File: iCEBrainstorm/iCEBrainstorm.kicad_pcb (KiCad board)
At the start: 4 copper layers, 80 x 70 mm, 117 parts, among them J1 Connector, USB-TYPE-C-16P, J10 Conn_01x02_Pin, J11 Conn_01x06_Pin, J12 Connector, USB-TYPE-C-16P, J2 Conn_01x06_Pin, J3 Conn_01x16_Pin, J6 Conn_01x03_Pin, J7 Conn_01x03_Pin, J8 Conn_01x02_Pin, J9 Conn_01x02_Pin, Q1 HL2312, SW1 SW_DIP_x08, U1 AMS1117-3.3, U2 AMS1117-1.2, U3 STM32F412RETx, U4 ICE40UP5K-SG48ITR, U5 W25Q128, X1 16 MHz

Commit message: gekocht mit luci
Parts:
- added C33: 100nF, PCM_JLCPCB:C_0603, F.Cu at (84.0, 113.9)
- added C34: 100nF, PCM_JLCPCB:C_0603, F.Cu at (80.8, 114.6)
- added R21: 1.5kΩ, PCM_JLCPCB:R_0603, F.Cu at (84.0, 110.4)
- added R22: 1.5kΩ, PCM_JLCPCB:R_0603, F.Cu at (77.5, 113.9)
- added R23: 1.5kΩ, PCM_JLCPCB:R_0603, F.Cu at (77.5, 110.4)
- added R24: 1.5kΩ, PCM_JLCPCB:R_0603, F.Cu at (80.8, 107.9)
- added U6: LSM6DS3, Package_LGA:LGA-14_3x2.5mm_P0.5mm_LayoutBorder3x4y, F.Cu at (80.8, 111.6)
- moved J11 113.5 mm to (69.8, 118.1), turned to 180 degrees
- moved D3 111.5 mm to (96.5, 68.6), turned to 90 degrees
- moved D2 108.7 mm to (99.1, 68.6), turned to 90 degrees
- moved D1 106.1 mm to (101.6, 68.6), turned to 90 degrees
- moved R6 104.0 mm to (96.5, 72.4), turned to -90 degrees
- moved D4 103.7 mm to (104.1, 68.6), turned to 90 degrees
- moved R5 101.6 mm to (99.1, 72.4), turned to -90 degrees
- moved R2 99.4 mm to (101.6, 72.4), turned to -90 degrees
- moved R30 97.4 mm to (104.1, 72.4), turned to 90 degrees
- moved J3 95.1 mm to (66.0, 80.0), turned to 0 degrees
- moved Q1 93.6 mm to (100.3, 76.2), turned to 90 degrees
- moved R1 88.2 mm to (100.3, 80.0), turned to 0 degrees
- moved C11 84.4 mm to (49.1, 22.2)
- moved C13 84.4 mm to (38.0, 20.0)
- moved C14 84.4 mm to (46.1, 38.2)
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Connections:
- U3 pad 50: /FPGA_BUS0 -> unconnected-(U3-PA15-Pad50)
- U3 pad 54: /FPGA_BUS1 -> unconnected-(U3-PD2-Pad54)
- U4 pad 10: unconnected-(U4B-IOB_18a-Pad10) -> /SPI2_SCK
- U4 pad 11: unconnected-(U4B-IOB_20a-Pad11) -> /SPI2_NSS
- U4 pad 23: /FPGA_BUS0 -> unconnected-(U4A-IOT_37a-Pad23)
- U4 pad 25: /FPGA_BUS1 -> unconnected-(U4A-IOT_36b-Pad25)
- U4 pad 28: /SPI2_MOSI -> unconnected-(U4A-IOT_41a-Pad28)
- U4 pad 31: /SPI2_MISO -> unconnected-(U4A-IOT_42b-Pad31)
- U4 pad 32: /SPI2_SCK -> unconnected-(U4A-IOT_43a-Pad32)
- U4 pad 34: /SPI2_NSS -> unconnected-(U4A-IOT_44b-Pad34)
- U4 pad 4: unconnected-(U4C-IOB_8a-Pad4) -> /SPI2_MOSI
- U4 pad 6: unconnected-(U4B-IOB_13b-Pad6) -> /SPI2_MISO
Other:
- board text added: "RESET STM"

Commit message: wider mit luci gekocht
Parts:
- moved C11 86.7 mm to (92.7, 97.2), turned to -135 degrees
- moved C16 86.4 mm to (81.8, 104.4)
- moved C18 86.4 mm to (81.8, 99.5)
- moved FB1 86.4 mm to (81.8, 102.0)
- moved C19 83.4 mm to (84.8, 97.5), turned to -135 degrees
- moved C8 81.3 mm to (98.3, 91.9), turned to -135 degrees
- moved C13 81.0 mm to (92.6, 79.9), turned to -45 degrees
- moved C14 75.7 mm to (97.3, 94.0), turned to 135 degrees
- moved R16 74.6 mm to (81.3, 78.7), turned to -90 degrees
- moved R15 73.0 mm to (79.8, 78.7), turned to -90 degrees
- moved R39 68.8 mm to (89.5, 74.3)
- moved D13 68.4 mm to (89.5, 78.1)
- moved C15 65.7 mm to (78.9, 90.3)
- moved C29 48.8 mm to (108.6, 80.0), turned to 90 degrees
- moved R7 48.0 mm to (123.4, 91.2)
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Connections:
- J3 pad 1: /PC0 -> /PA15
- J3 pad 10: +3V3 -> /PC15
- J3 pad 11: /PC10 -> /PC0
- J3 pad 12: /PC11 -> /PC1
- J3 pad 13: /PC12 -> /PC2
- J3 pad 14: /PC13 -> /PC3
- J3 pad 15: /PC14 -> /PA0
- J3 pad 16: /PC15 -> /PA1
- J3 pad 2: /PC1 -> /PC10
- J3 pad 3: /PC2 -> /PC11
- J3 pad 4: /PC3 -> /PC12
- J3 pad 5: /PC4 -> /PD2
- J3 pad 6: /PC5 -> /PB4
- J3 pad 7: /PC6 -> /PB9
- J3 pad 8: /PC7 -> /PC13
- J3 pad 9: /PC8 -> /PC14
- J8 pad 1: /FPGA_GLOBAL_3 -> unconnected-(J8-Pin_1-Pad1)
- J8 pad 2: /FPGA_GLOBAL_6 -> unconnected-(J8-Pin_2-Pad2)
- R18 pad 2: /IN1 -> /FPGA_GLOBAL_0
- R20 pad 2: /IN3 -> /FPGA_GLOBAL_1
- R25 pad 1: Net-(U4B-IOB_22a) -> /FPGA_GLOBAL_6
- R26 pad 1: Net-(U4B-IOB_22a) -> /FPGA_GLOBAL_6
- SW1 pad 6: /IN1 -> /FPGA_GLOBAL_0
- SW1 pad 8: /IN3 -> /FPGA_GLOBAL_1
- U3 pad 14: unconnected-(U3-PA0-Pad14) -> /PA0
- U3 pad 15: unconnected-(U3-PA1-Pad15) -> /PA1
- U3 pad 24: /PC4 -> unconnected-(U3-PC4-Pad24)
- U3 pad 25: /PC5 -> unconnected-(U3-PC5-Pad25)
- U3 pad 29: /FPGA_CLK -> /FPGA_GLOBAL_0
- U3 pad 37: /PC6 -> unconnected-(U3-PC6-Pad37)
- U3 pad 38: /PC7 -> unconnected-(U3-PC7-Pad38)
- U3 pad 39: /PC8 -> unconnected-(U3-PC8-Pad39)
- U3 pad 50: unconnected-(U3-PA15-Pad50) -> /PA15
- U3 pad 54: unconnected-(U3-PD2-Pad54) -> /PD2
- U3 pad 56: unconnected-(U3-PB4-Pad56) -> /PB4
- U3 pad 62: unconnected-(U3-PB9-Pad62) -> /PB9
- U4 pad 12: Net-(U4B-IOB_22a) -> unconnected-(U4B-IOB_22a-Pad12)
- U4 pad 13: /FUD- -> unconnected-(U4B-IOB_24a-Pad13)
- U4 pad 2: /OUT1 -> /USART1_RX
- U4 pad 20: /FPGA_GLOBAL_3 -> /FPGA_CLK
- U4 pad 21: /FUD+ -> unconnected-(U4B-IOB_23b-Pad21)
- U4 pad 25: unconnected-(U4A-IOT_36b-Pad25) -> /OUT0
- U4 pad 26: /USART1_RX -> /OUT1
- U4 pad 27: /USART1_TX -> /OUT2
- U4 pad 28: unconnected-(U4A-IOT_41a-Pad28) -> /OUT3
- U4 pad 3: /OUT0 -> /USART1_TX
- U4 pad 31: unconnected-(U4A-IOT_42b-Pad31) -> /BTN0
- U4 pad 32: unconnected-(U4A-IOT_43a-Pad32) -> /BTN1
- U4 pad 34: unconnected-(U4A-IOT_44b-Pad34) -> /IN0
- U4 pad 35: /FPGA_CLK -> /FPGA_GLOBAL_0
- U4 pad 36: /BTN0 -> /IN2
- U4 pad 38: /BTN1 -> unconnected-(U4A-IOT_50b-Pad38)
- U4 pad 45: unconnected-(U4C-IOB_5b-Pad45) -> /FUD-
- U4 pad 47: /OUT3 -> unconnected-(U4C-IOB_2a-Pad47)
- U4 pad 48: /OUT2 -> /FUD+
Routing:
- net GND: track 0.00 -> 82.8 mm, vias 0 -> 15
- net +3V3: track 0.00 -> 54.4 mm, vias 0 -> 9
- net /PA1: track 0.00 -> 33.6 mm, vias 0 -> 1
- net /PC3: track 0.00 -> 32.3 mm, vias 0 -> 1
- net /PA0: track 0.00 -> 31.3 mm, vias 0 -> 1
- net /PD2: track 0.00 -> 28.6 mm, vias 0 -> 1
- net /PB4: track 0.00 -> 28.6 mm, vias 0 -> 1
- net /PC11: track 0.00 -> 28.4 mm, vias 0 -> 1
- net /PC10: track 0.00 -> 28.4 mm, vias 0 -> 1
- net /PC12: track 0.00 -> 28.2 mm, vias 0 -> 1
- net /PC2: track 0.00 -> 28.2 mm, vias 0 -> 1
- net VBUS: track 0.00 -> 27.9 mm, vias 0 -> 8
- net /PA15: track 0.00 -> 27.6 mm, vias 0 -> 1
- net /PC1: track 0.00 -> 25.8 mm, vias 0 -> 1
- net /PC0: track 0.00 -> 24.6 mm, vias 0 -> 1
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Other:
- board text added: "OUT_STM"
- board text added: "PA0"
- board text added: "PA1"
- board text added: "PA15"
- board text added: "PB4"
- board text added: "PB9"
- board text added: "PD2"
- board text removed: "FPGA"
- board text removed: "G3"
- board text removed: "G6"
- board text removed: "OUT8"
- board text removed: "PC4"
- board text removed: "PC5"
- board text removed: "PC6"
- board text removed: "PC7"
- board text removed: "PC8"

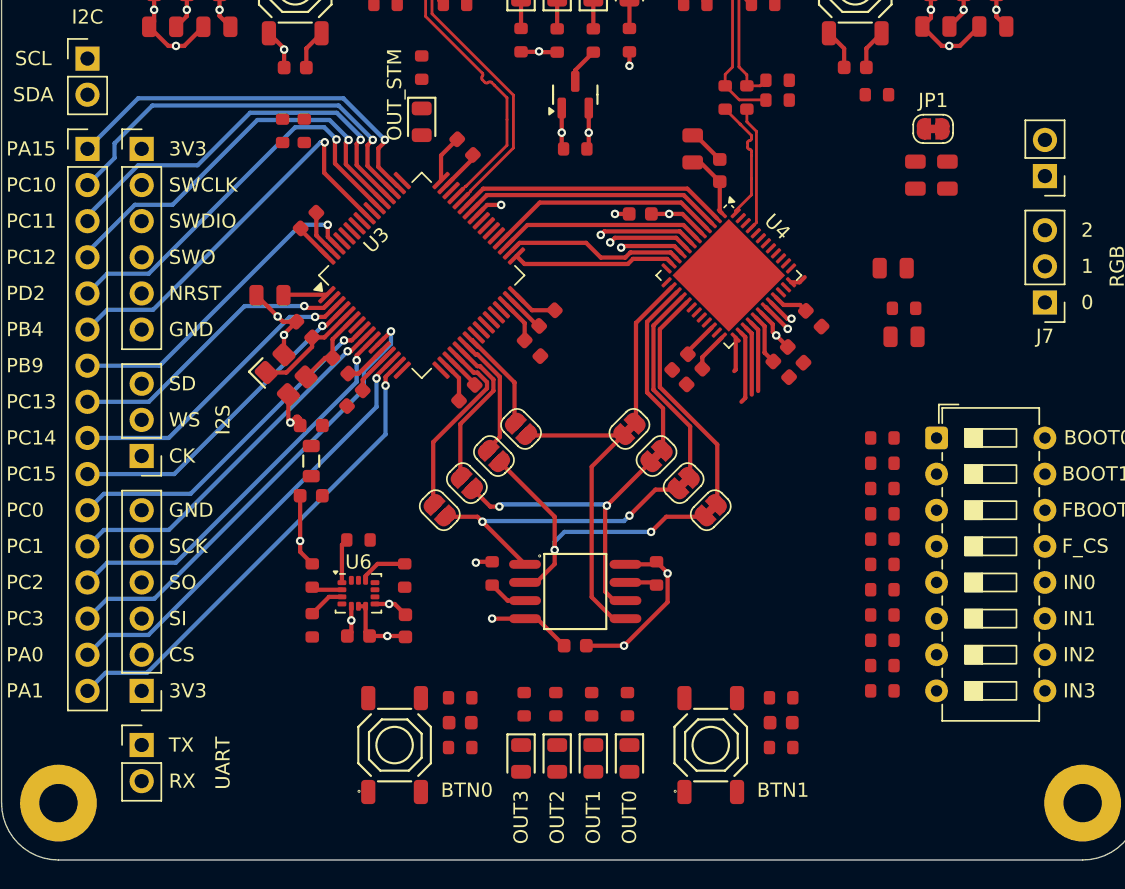
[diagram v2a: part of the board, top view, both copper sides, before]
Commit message: did some lines + added a IN connector :)
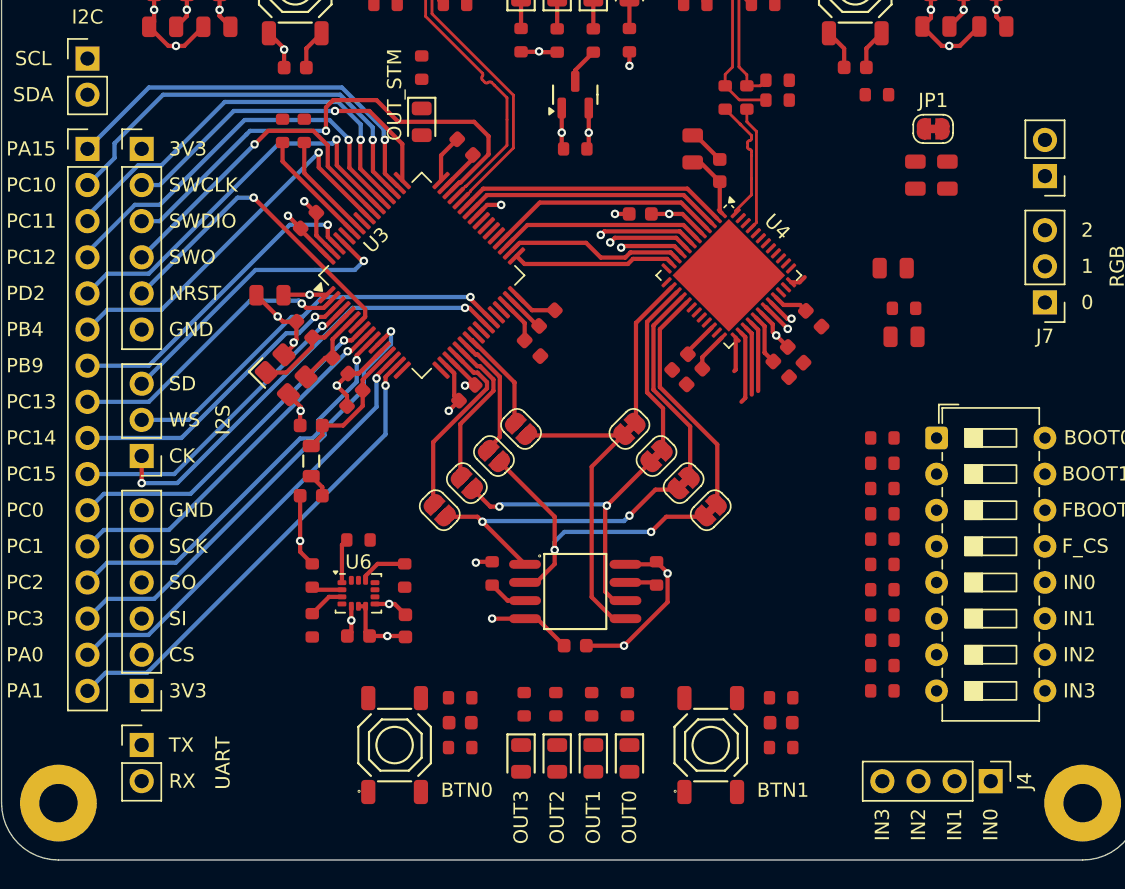
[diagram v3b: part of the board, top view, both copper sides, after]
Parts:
- added J4: Conn_01x04_Pin, Connector_PinHeader_2.54mm:PinHeader_1x04_P2.54mm_Vertical, F.Cu at (129.5, 124.5)
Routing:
- net /SWDIO: track 0.00 -> 34.9 mm, vias 0 -> 1
- net /I2S5_CK: track 0.00 -> 31.7 mm, vias 0 -> 2
- net /I2S5_WS: track 0.00 -> 28.9 mm, vias 0 -> 1
- net /SWCLK: track 0.00 -> 24.0 mm, vias 0 -> 1
- net /NRST: track 2.86 -> 25.9 mm, vias 0 -> 1
- net /SWO: track 0.00 -> 23.1 mm, vias 0 -> 1
- net /I2S5_SD: track 0.00 -> 21.3 mm, vias 0 -> 1
- net /I2C1_SDA: track 0.00 -> 8.23 mm
- net /I2C1_SCL: track 0.00 -> 7.39 mm
- net +3.3VA: track 3.20 -> 9.46 mm
- net GND: track 82.8 -> 87.1 mm, vias 15 -> 18
- net +3V3: track 54.4 -> 58.1 mm, vias 9 -> 12
- net /PB4: track 28.6 -> 27.3 mm
- net /PC11: track 28.4 -> 29.4 mm
- net /PC10: track 28.4 -> 29.3 mm
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
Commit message: did back silkscreen design
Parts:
- added REF**: iCE-Brain, JJ:iCE-Brain, F.Cu at (100.8, 96.1)

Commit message: added uart1 connector, added power connectors, added schema back silkscreen symbol
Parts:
- removed REF**: iCE-Brain, JJ:iCE-Brain
- added J13: Conn_01x02_Pin, Connector_PinHeader_2.54mm:PinHeader_1x02_P2.54mm_Vertical, F.Cu at (157.5, 131.4)
- added J14: Conn_01x02_Pin, Connector_PinHeader_2.54mm:PinHeader_1x02_P2.54mm_Vertical, F.Cu at (157.5, 139.1)
- added J15: Conn_01x02_Pin, Connector_PinHeader_2.54mm:PinHeader_1x02_P2.54mm_Vertical, F.Cu at (157.5, 146.7)
- added J5: Conn_01x02_Pin, Connector_PinHeader_2.54mm:PinHeader_1x02_P2.54mm_Vertical, F.Cu at (104.1, 80.6)
- added N1: Housing, iCE-Brain Silkscreen, JJ:iCE-Brain, F.Cu at (101.0, 96.1)
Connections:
- U3 pad 24: unconnected-(U3-PC4-Pad24) -> /FPGA_BUS1
- U3 pad 25: unconnected-(U3-PC5-Pad25) -> /FPGA_BUS0
- U4 pad 12: unconnected-(U4B-IOB_22a-Pad12) -> /FPGA_BUS0
- U4 pad 13: unconnected-(U4B-IOB_24a-Pad13) -> /FPGA_BUS1
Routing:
- net /FPGA_BUS1: track 0.00 -> 17.5 mm
- net /FPGA_BUS0: track 0.00 -> 17.3 mm
- net /USART1_RX: track 19.0 -> 25.8 mm
- net /USART1_TX: track 18.2 -> 22.6 mm, vias 0 -> 1
- net +3V3: vias 12 -> 13
- net GND: vias 18 -> 19
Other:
- board text added: "UART1"
- board text added: "UART2"
- board text removed: "UART"

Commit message: did some routing
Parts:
- removed J8: Conn_01x02_Pin, Connector_PinHeader_2.54mm:PinHeader_1x02_P2.54mm_Vertical
- moved J13 88.0 mm to (69.8, 123.2)
- moved J14 63.8 mm to (133.3, 80.0)
- moved J15 59.1 mm to (133.3, 92.7)
- moved C9 10.3 mm to (114.8, 98.8), turned to -90 degrees
- moved R7 9.46 mm to (116.7, 97.9), turned to 90 degrees
- moved C22 6.16 mm to (128.8, 76.1), turned to 0 degrees
- moved C5 5.74 mm to (128.8, 78.4), turned to 0 degrees
- moved C23 4.19 mm to (121.7, 92.5), turned to -90 degrees
- moved J10 3.81 mm to (69.8, 118.1)
- moved J11 2.54 mm to (69.8, 115.6)
- moved JP1 1.46 mm to (125.6, 77.1), turned to -90 degrees
- moved J9 1.27 mm to (66.0, 74.9)
- moved J6 1.27 mm to (69.8, 100.3)
- moved J7 0.64 mm to (133.3, 90.2)
- moved C26 0.28 mm to (115.6, 94.4)
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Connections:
- U3 pad 41: /FPGA_GLOBAL_1 -> /FPGA_GLOBAL_6
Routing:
- net /I2C1_SCL: track 7.39 -> 82.7 mm, vias 0 -> 6
- net /I2C1_SDA: track 8.23 -> 79.0 mm, vias 0 -> 4
- net /BTN0: track 2.16 -> 65.3 mm, vias 1 -> 0
- net /BOOT0: track 0.00 -> 52.9 mm, vias 0 -> 1
- net /IN0: track 0.00 -> 50.4 mm, vias 0 -> 1
- net /FPGA_GLOBAL_0: track 0.00 -> 49.5 mm, vias 0 -> 1
- net /IN2: track 1.11 -> 50.2 mm, vias 0 -> 1
- net /FPGA_GLOBAL_1: track 2.07 -> 49.1 mm
- net /FPGA_SPI_CS: track 21.5 -> 68.4 mm
- net /BOOT1: track 0.00 -> 42.1 mm, vias 0 -> 1
- net /OUT3: track 5.03 -> 46.3 mm
- net /OUT2: track 4.89 -> 42.4 mm
- net /USART2_RX: track 0.00 -> 33.8 mm, vias 0 -> 1
- net /BTN1: track 1.92 -> 35.6 mm, vias 1 -> 0
- net /OUT1: track 5.11 -> 38.5 mm
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- added copper zone on In2.Cu, net +3V3
- added copper zone on In1.Cu, net GND

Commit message: fertig
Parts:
- added J11: Conn_01x04_Pin, Connector_PinHeader_2.54mm:PinHeader_1x04_P2.54mm_Vertical, F.Cu at (133.3, 74.9)
- moved J5 10.2 mm to (133.3, 69.8)
- renumbered D13 to D9, J7 to J10, J9 to J12, J10 to J13, J5 to J14, J11 to J15, J12 to J16, J3 to J2, J2 to J3, J13 to J4, J14 to J5, J15 to J6, J4 to J7, J6 to J9, JP8 to JP6, JP9 to JP7, JP10 to JP8, JP11 to JP9, R17 to R11, R18 to R12, R19 to R13, R20 to R14, R11 to R15, R12 to R16, R13 to R17, R14 to R18, R15 to R19, R16 to R20, R29 to R21, R30 to R22, R31 to R23, R32 to R24, R33 to R25, R34 to R26, R39 to R27, R40 to R28, R41 to R29, R42 to R30, R43 to R31, R44 to R32, R45 to R33, R24 to R34, R23 to R35, R22 to R36, R46 to R37, R47 to R38, R25 to R39, R26 to R40, R21 to R41, R27 to R42, R28 to R43
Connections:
- R39 pad 1: /FPGA_GLOBAL_6 -> /FUPP
- R40 pad 1: /FPGA_GLOBAL_6 -> /FUPP
- U3 pad 29: /FPGA_GLOBAL_0 -> unconnected-(U3-PB10-Pad29)
- U4 pad 23: unconnected-(U4A-IOT_37a-Pad23) -> /FPGA_IO_3
- U4 pad 38: unconnected-(U4A-IOT_50b-Pad38) -> /FPGA_IO_2
- U4 pad 42: unconnected-(U4A-IOT_51a-Pad42) -> /FPGA_IO_1
- U4 pad 43: unconnected-(U4A-IOT_49a-Pad43) -> /FUPP
- U4 pad 47: unconnected-(U4C-IOB_2a-Pad47) -> /FPGA_IO_0
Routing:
- net +1V2: track 24.2 -> 100.0 mm
- net VBUS: track 27.9 -> 97.9 mm
- net /FPGA_BOOT: track 8.34 -> 49.1 mm
- net /FPGA_IO_3: track 0.00 -> 30.0 mm, vias 0 -> 3
- net /FPGA_IO_0: track 0.00 -> 26.8 mm, vias 0 -> 1
- net +2V5: track 6.66 -> 30.6 mm
- net /FPGA_IO_1: track 0.00 -> 23.4 mm
- net /FPGA_IO_2: track 0.00 -> 21.6 mm, vias 0 -> 1
- net /FUPP: track 0.00 -> 11.9 mm
- net +3V3: track 68.8 -> 75.5 mm, vias 26 -> 27
- net GND: track 119.0 -> 124.0 mm, vias 41 -> 49
- net /VCCPLL: track 9.98 -> 14.2 mm
- net /PB9: track 25.0 -> 22.7 mm
- net /IN2: track 50.2 -> 49.1 mm
- net /FPGA_SPI_SCK: track 47.6 -> 48.3 mm
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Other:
- board text added: "3"
- board text added: "F-CS"
- board text added: "FPGA-IO"
- board text removed: "F_CS"
